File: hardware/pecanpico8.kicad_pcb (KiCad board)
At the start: 4 copper layers, 29.8 x 44.7 mm, 149 parts, among them IC1 SPV1040, IC2 TPS62260, IC3 ADP322ACPZ-115-R7, IC4 Si4464, IC5 STM32F745IGKx, IC6 EVA-7M, IC7 PAC1720, IC8 BME280, IC9 BME280, P1 CONN_02X13, P2 CONN_01X11, P3 USB_OTG, P4 IPX 2mm, P5 CONN_01X02, P6 IPX 2mm, P7 CONN_02X13, Q1 FDN306P, U1 AS-213, U2 LFCN-120, U3 uctronics OV2640, X1 KT2016K26000BCW18ZAS

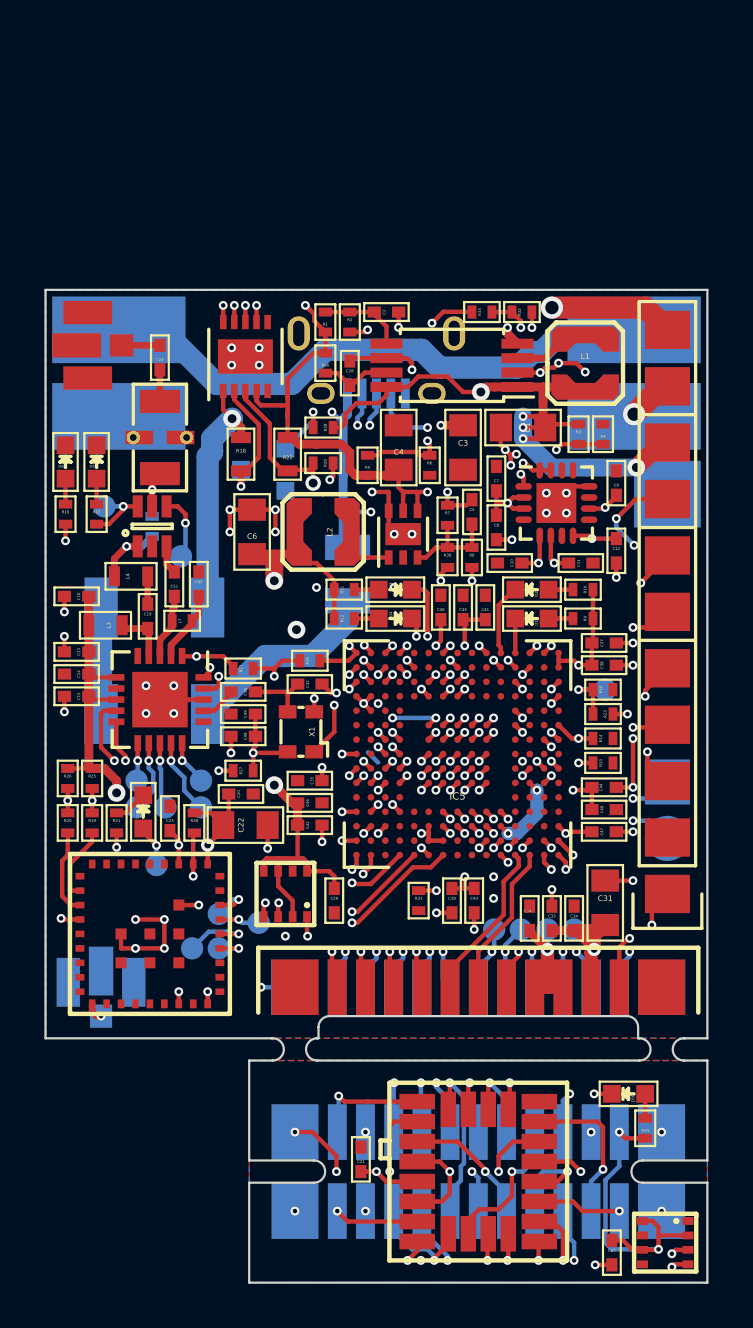
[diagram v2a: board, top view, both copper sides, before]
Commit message: Added new LDO for GPS Implemented constant voltage for LEDs Replaced MicroUSB THT connector with SMD connector Replaced LPF
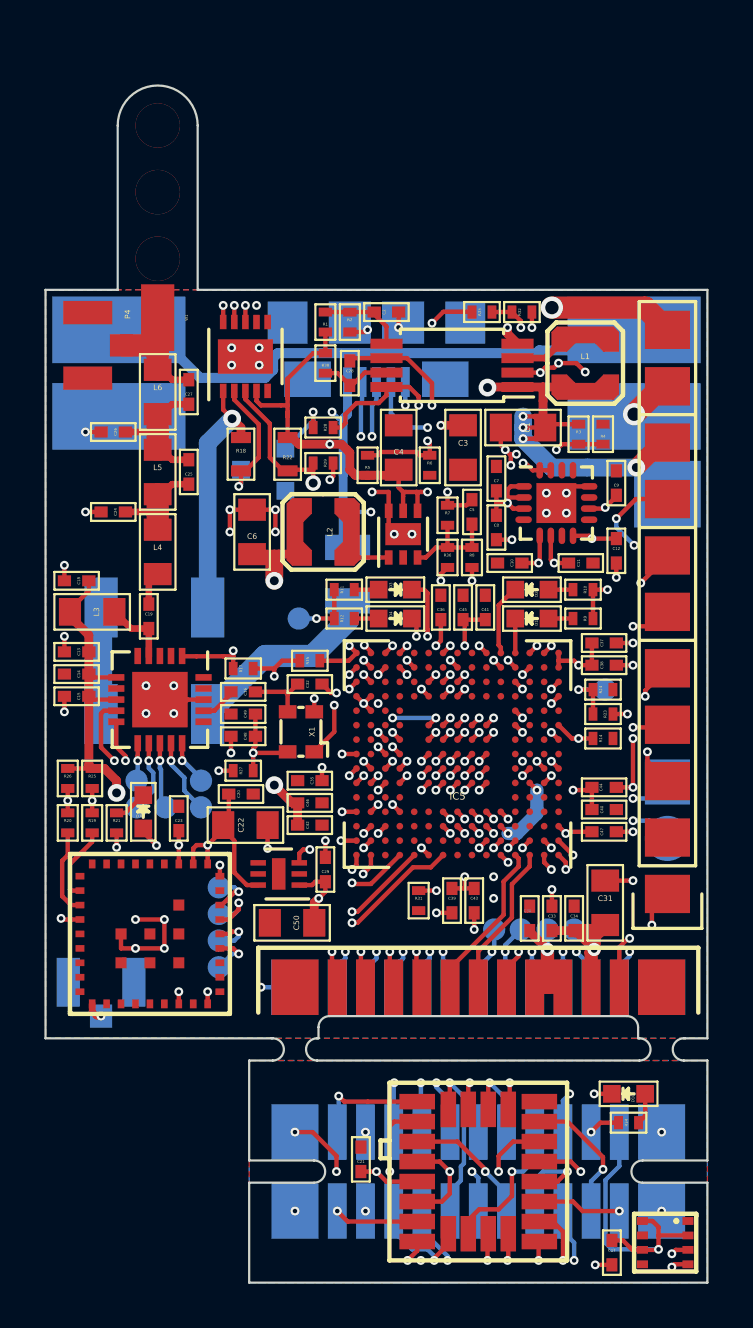
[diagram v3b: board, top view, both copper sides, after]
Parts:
- removed C51: 470p, stm32f7:C_0402
- removed D5: red, stm32f7:LED_0603
- removed D6: green, stm32f7:LED_0603
- removed L7: 56n, stm32f7:R_0402
- removed R13: 100k, stm32f7:R_0402
- removed R15: 1k5, stm32f7:R_0402
- removed R16: 330R, stm32f7:R_0402
- removed R37, R38: 0R, stm32f7:R_0402
- removed U1: AS-213, stm32f7:SC-70-6
- removed U2: LFCN-120, stm32f7:FV1206
- removed W3: Testpad, stm32f7:Testpad
- added C25: 470p, stm32f7:C_0402, F.Cu at (53.5, 99.1)
- added C26: 22p, stm32f7:C_0402, F.Cu at (50.1, 97.3)
- added C27: 470p, stm32f7:C_0402, F.Cu at (53.5, 95.5)
- added L5: 82n, stm32f7:C_0805, F.Cu at (52.1, 99.1)
- added L6: 56n, stm32f7:C_0805, F.Cu at (52.1, 95.5)
- added REF**: MountingHole_2-5mm, Mounting_Holes:MountingHole_2-5mm, F.Cu at (52.1, 89.5)
- added REF**: MountingHole_2-5mm, Mounting_Holes:MountingHole_2-5mm, F.Cu at (52.1, 86.5)
- added REF**: MountingHole_2-5mm, Mounting_Holes:MountingHole_2-5mm, F.Cu at (52.1, 83.5)
- C24: value 470p -> 22p
- C50: value 470p -> 22u; footprint stm32f7:C_0402 -> stm32f7:C_0805
- D1: value green -> yellow
- D2: value green -> blue
- D4: value green -> red
- IC8: value BME280 -> LDLN015PU30R; footprint stm32f7:BME280 -> Housings_DFN_QFN:DFN-6-1EP_2x2mm_Pitch0.5mm
- L3, L4: footprint stm32f7:R_0603 -> stm32f7:C_0805
- P3: value USB_OTG -> ZX62-B-5PA(33); footprint stm32f7:USB_Micro-B -> stm32f7:USB_Micro-B_SMD
- R21: value 1k5 -> 1k
- W1: footprint stm32f7:Testpad -> stm32f7:PAD_3x1.5; moved to F.Cu
- moved C50 15.8 mm to (58.2, 119.4), turned to 180 degrees
- moved W21 12.8 mm to (58.5, 105.7)
- moved W1 8.83 mm to (52.1, 92.2), turned to 90 degrees
- moved C24 7.26 mm to (50.1, 100.9), turned to 180 degrees
- moved W17 1.84 mm to (54.9, 119.0)
- moved L4 1.63 mm to (52.1, 102.7), turned to 270 degrees
- moved C29 1.46 mm to (59.7, 117.0), turned to 90 degrees
- moved W19 1.25 mm to (54.9, 120.2)
- moved W15 1.20 mm to (54.9, 117.8)
- moved IC8 0.95 mm to (57.6, 117.2), turned to 180 degrees
- moved W20 0.85 mm to (54.9, 121.4)
- moved L3 0.85 mm to (49.2, 105.4)
- moved R34 0.79 mm to (73.3, 128.4), turned to 0 degrees
- moved C18 0.70 mm to (48.5, 104.0)
- moved P3 0.50 mm to (62.0, 93.5)
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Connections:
- C20 pad 1: +3V3 -> /VCC_GPS
- C22 pad 1: +3V3 -> /VCC_GPS
- C24 pad 2: Net-(C24-Pad2) -> GND
- C29 pad 1: +1V8 -> VDD
- C3 pad 1: /SENSE_BAT- -> VDD
- C4 pad 1: /SENSE_BAT- -> VDD
- C50 pad 1: GND -> VDD
- C50 pad 2: Net-(C50-Pad2) -> GND
- C7 pad 1: /SENSE_BAT- -> VDD
- C8 pad 1: /SENSE_BAT- -> VDD
- C9 pad 1: /SENSE_BAT- -> VDD
- D7 pad 2: +3V3 -> /VCC_GPS
- IC1 pad 4: /SENSE_BAT- -> VDD
- IC2 pad 4: /SENSE_BAT- -> VDD
- IC2 pad 5: /SENSE_BAT- -> VDD
- IC3 pad 1: /GPS_EN -> VDD
- IC3 pad 10: /SENSE_BAT- -> VDD
- IC3 pad 2: /SENSE_BAT- -> VDD
- IC3 pad 3: /SENSE_BAT- -> VDD
- IC4 pad 19: /RADIO_GPIO2 -> (no net)
- IC4 pad 2: Net-(C50-Pad2) -> (no net)
- IC4 pad 20: /RADIO_GPIO3 -> (no net)
- IC4 pad 3: Net-(C51-Pad1) -> (no net)
- IC5 pad B10: +IO -> (no net)
- IC5 pad B14: (no net) -> /GPS_EN
- IC5 pad B9: +IO -> (no net)
- IC5 pad C10: +IO -> (no net)
- IC5 pad J2: /GPS_EN -> (no net)
- IC5 pad N13: /PAC_ALERT -> (no net)
- IC6 pad 19: +3V3 -> /VCC_GPS
- IC6 pad 20: +IO -> /VCC_GPS
- IC7 pad 10: /SENSE_BAT- -> +3V3
- IC7 pad 4: /SENSE_BAT- -> VDD
- IC7 pad 7: /PAC_ALERT -> (no net)
- IC8 pad 1: GND -> VDD
- IC8 pad 2: +1V8 -> (no net)
- IC8 pad 3: /I2C_SDA -> /GPS_EN
- IC8 pad 4: /I2C_SCL -> GND
- IC8 pad 5: +1V8 -> (no net)
- IC8 pad 6: +1V8 -> /VCC_GPS
- L4 pad 1: Net-(L4-Pad1) -> Net-(C24-Pad1)
- P4 pad 1: Net-(C24-Pad2) -> Net-(C27-Pad2)
- R1 pad 1: /SENSE_BAT- -> VDD
- R10 pad 1: +1V8 -> +3V3
- R11 pad 1: +1V8 -> +3V3
- R12 pad 1: +1V8 -> +3V3
- R22 pad 2: /SENSE_BAT- -> VDD
- R30 pad 2: /SENSE_BAT- -> VDD
- R34 pad 1: +1V8 -> /OV2640_AVDD
- R5 pad 1: /SENSE_BAT- -> VDD
- R9 pad 1: +1V8 -> +3V3
- W1 pad 1: /RADIO_GPIO2 -> Net-(C27-Pad2)
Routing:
- net VDD: track 0.00 -> 69.0 mm, vias 0 -> 7
- net /SENSE_BAT-: track 49.4 -> 0.00 mm, vias 7 -> 0
- net /PAC_ALERT: track 22.8 -> 0.00 mm, vias 4 -> 0
- net /RADIO_GPIO3: track 20.9 -> 0.00 mm, vias 3 -> 0
- net /RADIO_GPIO2: track 18.6 -> 0.00 mm, vias 2 -> 0
- net +IO: track 16.2 -> 0.00 mm, vias 2 -> 0
- net +1V8: track 164.4 -> 148.9 mm, vias 33 -> 32
- net /GPS_EN: track 17.8 -> 4.84 mm, vias 3 -> 2
- net /VCC_GPS: track 0.00 -> 12.1 mm, vias 0 -> 2
- net Net-(C25-Pad2): track 0.00 -> 6.22 mm
- net Net-(C27-Pad2): track 0.00 -> 5.69 mm
- net +3V3: track 36.2 -> 40.9 mm, vias 4 -> 5
- net /I2C_SCL: track 63.4 -> 59.4 mm, vias 5 -> 4
- net Net-(L4-Pad1): track 3.41 -> 0.00 mm, vias 1 -> 0
- net +SOL: track 53.7 -> 50.4 mm, vias 6 -> 7
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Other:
- board size 29.8 x 44.7 mm -> 29.8 x 53.9 mm
- net class Power: clearance 0.1 -> 0.15; trace_width 0.2 -> 0.45
- board text added: "+3.3V"
- board text added: "March 2017"
- board text removed: "Jan 2017"
- board text removed: "VCC GPS"

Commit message: Moving parts around
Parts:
- moved D9 6.81 mm to (51.7, 103.2)
- moved F1 5.50 mm to (56.3, 100.4)
- moved D8 5.21 mm to (51.7, 100.0)
- moved C50 3.40 mm to (61.5, 118.4), turned to 0 degrees
- moved C29 2.90 mm to (57.6, 119.0), turned to 180 degrees
- moved Q1 2.78 mm to (55.5, 96.6)
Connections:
- D8 pad 1: +SOL -> Net-(D8-Pad1)
- D9 pad 2: Net-(D9-Pad2) -> /USB_VUSB
- F1 pad 1: Net-(D9-Pad2) -> Net-(D8-Pad1)
- F1 pad 2: /USB_VUSB -> +SOL
- IC5 pad A11: /GPS_RESET -> /GPS_TIMEPULSE
- IC5 pad A9: /GPS_TIMEPULSE -> /GPS_RESET
- IC9 pad 5: GND -> +1V8
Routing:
- net Net-(D9-Pad2): track 8.94 -> 0.00 mm
- net /USB_VUSB: track 25.7 -> 33.3 mm
- net /SWD_SWCLK: track 24.0 -> 18.0 mm
- net +SOL: track 50.4 -> 44.6 mm
- net Net-(D8-Pad1): track 0.00 -> 2.98 mm
- net /SENSE_SOL-: track 6.04 -> 8.13 mm
- net /GPS_RESET: track 11.4 -> 13.4 mm
- net Net-(D8-Pad2): track 4.80 -> 3.20 mm
- net GND: track 88.0 -> 86.4 mm, vias 110 -> 107
- net /CAM_D9: track 8.84 -> 10.2 mm
- net /GPS_TIMEPULSE: track 23.8 -> 22.5 mm
- net /SWD_SWDIO: track 18.9 -> 17.6 mm
- net /SOL_SHORT_EN: track 18.6 -> 19.7 mm
- net /CAM_EN: track 17.9 -> 16.9 mm
- net VDD: track 69.0 -> 69.8 mm
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
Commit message: Moving parts around
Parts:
- moved C25 4.20 mm to (49.4, 99.1)
- moved C24 1.41 mm to (48.8, 100.7)
- moved C26 1.41 mm to (48.8, 97.5)
- moved L5 1.40 mm to (50.8, 99.1)
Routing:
- net GND: track 86.4 -> 88.6 mm, vias 107 -> 110
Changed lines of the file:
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@@
     (links 460)
     (no_connects 2)
-    (area 37.303263 78.92488 87.9 135.843)
+    (area 47.049999 81.649999 76.950001 135.650001)
     (thickness 1)
     (drawings 85)
-    (tracks 1869)
+    (tracks 1881)
     (zones 0)
     (modules 145)
@@
     (add_net "Net-(W6-Pad1)")
   )
+  (module stm32f7:PAD_6x3 (layer B.Cu)
+    (at 50.4 96.6)
+    (fp_text reference W10 (at 0 -3) (layer B.SilkS) hide
+      (effects (font (size 0.5 0.5) (thickness 0.075)) (justify mirror))
+    )
+    (fp_text value Pad (at 0 -2.2) (layer B.Fab) hide
+      (effects (font (size 0.5 0.5) (thickness 0.075)) (justify mirror))
+    )
+    (pad 1 smd rect (at 0 0) (size 6 3) (layers B.Cu B.Mask)
+      (net 2 GND) (zone_connect 2))
+  )
   (module stm32f7:Pin_Header_Straight_1x11 (layer F.Cu)
     (at 75.1 118.1 180)
@@
       (net 83 /BATT_CONN))
   )
-  (module stm32f7:PAD_6x3 (layer B.Cu)
-    (at 50.4 96.6)
-    (fp_text reference W10 (at 0 -3) (layer B.SilkS) hide
-      (effects (font (size 0.5 0.5) (thickness 0.075)) (justify mirror))
-    )
-    (fp_text value Pad (at 0 -2.2) (layer B.Fab) hide
-      (effects (font (size 0.5 0.5) (thickness 0.075)) (justify mirror))
-    )
-    (pad 1 smd rect (at 0 0) (size 6 3) (layers B.Cu B.Mask)
-      (net 2 GND) (zone_connect 2))
-  )
   (module stm32f7:R_0402 (layer F.Cu)
     (at 61.6 98.8 90)
@@
   )
   (module stm32f7:C_0402 (layer F.Cu)
-    (at 53.55 99.1 90)
+    (at 49.35 99.1 90)
     (descr "Capacitor SMD 0402, reflow soldering, AVX (see smccp.pdf)")
     (tags "capacitor 0402")
@@
   )
   (module stm32f7:C_0402 (layer F.Cu)
-    (at 50.15 97.3 180)
+    (at 48.75 97.5 180)
     (descr "Capacitor SMD 0402, reflow soldering, AVX (see smccp.pdf)")
     (tags "capacitor 0402")
@@
   )
   (module stm32f7:C_0805 (layer F.Cu)
-    (at 52.15 99.1 270)
+    (at 50.75 99.1 270)
     (descr "Capacitor SMD 0805, reflow soldering, AVX (see smccp.pdf)")
     (tags "capacitor 0805")
@@
   )
   (module stm32f7:C_0402 (layer F.Cu)
-    (at 50.15 100.9 180)
+    (at 48.75 100.7 180)
     (descr "Capacitor SMD 0402, reflow soldering, AVX (see smccp.pdf)")
     (tags "capacitor 0402")
@@
   (module stm32f7:PAD_3x1.5 (layer F.Cu)
     (at 52.15 92.15 90)
-    (fp_text reference W1 (at 0 1.3 90) (layer F.SilkS)
+    (fp_text reference W1 (at 0 1.3 90) (layer F.SilkS) hide
       (effects (font (size 0.127 0.127) (thickness 0.01875)))
     )
@@
   (module stm32f7:IPX_2mm (layer F.Cu)
     (at 49 93.4)
-    (fp_text reference P4 (at 1.8 -1.4 270) (layer F.SilkS)
+    (fp_text reference P4 (at 1.8 -1.4 90) (layer F.SilkS) hide
       (effects (font (size 0.25 0.25) (thickness 0.0375)))
     )
@@
   (segment (start 65.4 117.85) (end 65.975 117.85) (width 0.2) (layer F.Cu) (net 1))
   (segment (start 65.975 117.325) (end 65.975 117.85) (width 0.2) (layer F.Cu) (net 1))
+  (segment (start 48.2 97.5) (end 48.2 96.9) (width 0.2) (layer F.Cu) (net 2))
+  (segment (start 48.2 96.9) (end 48.1 96.8) (width 0.2) (layer F.Cu) (net 2))
+  (via (at 48.1 96.8) (size 0.4) (drill 0.2) (layers F.Cu B.Cu) (net 2))
+  (segment (start 48.2 100.7) (end 48.2 100.1) (width 0.2) (layer F.Cu) (net 2))
+  (segment (start 48.2 100.1) (end 48.1 100) (width 0.2) (layer F.Cu) (net 2))
+  (via (at 48.1 100) (size 0.4) (drill 0.2) (layers F.Cu B.Cu) (net 2))
+  (segment (start 48.2 97.5) (end 48.2 98.1) (width 0.2) (layer F.Cu) (net 2))
+  (segment (start 48.2 98.1) (end 48.1 98.2) (width 0.2) (layer F.Cu) (net 2))
+  (via (at 48.1 98.2) (size 0.4) (drill 0.2) (layers F.Cu B.Cu) (net 2))
+  (segment (start 48.2 100.7) (end 48.2 101.3) (width 0.2) (layer F.Cu) (net 2))
+  (segment (start 48.2 101.3) (end 48.1 101.4) (width 0.2) (layer F.Cu) (net 2))
+  (via (at 48.1 101.4) (size 0.4) (drill 0.2) (layers F.Cu B.Cu) (net 2))
   (segment (start 49.85 123.05) (end 49.85 122.5) (width 0.2) (layer F.Cu) (net 2))
   (via (at 49.85 122.5) (size 0.4) (drill 0.2) (layers F.Cu B.Cu) (net 2))
@@
   (segment (start 63.3 95.05) (end 63.3 96.1) (width 0.2) (layer B.Cu) (net 2))
   (via (at 63.3 96.1) (size 0.4) (drill 0.2) (layers F.Cu B.Cu) (net 2))
-  (segment (start 48.9 97.3) (end 49.6 97.3) (width 0.2) (layer F.Cu) (net 2))
-  (via (at 48.9 97.3) (size 0.4) (drill 0.2) (layers F.Cu B.Cu) (net 2))
   (segment (start 54.95 117.3) (end 54.95 116.8) (width 0.2) (layer F.Cu) (net 2))
   (via (at 54.95 116.8) (size 0.4) (drill 0.2) (layers F.Cu B.Cu) (net 2))
@@
   (segment (start 75.1 95.24) (end 75.04 95.24) (width 1) (layer F.Cu) (net 83))
   (segment (start 74.9476 95.24) (end 75.1 95.24) (width 1) (layer F.Cu) (net 83))
-  (segment (start 52.15 100.1) (end 52.15 100.9) (width 1) (layer F.Cu) (net 84))
-  (segment (start 52.15 100.9) (end 52.15 101.7) (width 1) (layer F.Cu) (net 84))
-  (segment (start 50.7 100.9) (end 52.15 100.9) (width 0.3) (layer F.Cu) (net 84))
-  (segment (start 53.55 99.65) (end 52.8 99.65) (width 0.3) (layer F.Cu) (net 84))
-  (segment (start 52.15 100.1) (end 52.35 100.1) (width 0.3) (layer F.Cu) (net 84))
-  (segment (start 52.35 100.1) (end 52.8 99.65) (width 0.3) (layer F.Cu) (net 84))
+  (segment (start 49.35 99.65) (end 49.35 100.1) (width 0.4) (layer F.Cu) (net 84))
+  (segment (start 49.35 100.1) (end 49.35 100.65) (width 0.4) (layer F.Cu) (net 84))
+  (segment (start 50.75 100.1) (end 49.35 100.1) (width 0.4) (layer F.Cu) (net 84))
+  (segment (start 49.35 100.65) (end 49.3 100.7) (width 0.4) (layer F.Cu) (net 84))
+  (segment (start 50.75 100.3) (end 51.2 100.75) (width 1) (layer F.Cu) (net 84))
+  (segment (start 51.2 100.75) (end 52.15 101.7) (width 1) (layer F.Cu) (net 84))
+  (segment (start 50.75 100.1) (end 50.75 100.3) (width 1) (layer F.Cu) (net 84))
   (segment (start 68.4 116.866002) (end 68.4 116.5) (width 0.2) (layer F.Cu) (net 85))
   (segment (start 68.25 116.35) (end 68.4 116.5) (width 0.2) (layer F.Cu) (net 85))
@@
   (segment (start 68.15 100.75) (end 67.9 100.5) (width 0.2) (layer F.Cu) (net 110))
   (via (at 67.9 100.5) (size 0.4) (drill 0.2) (layers F.Cu B.Cu) (net 110))
-  (segment (start 52.15 96.5) (end 52.15 97.3) (width 1) (layer F.Cu) (net 111))
-  (segment (start 52.15 97.3) (end 52.15 98.1) (width 1) (layer F.Cu) (net 111))
-  (segment (start 50.7 97.3) (end 52.15 97.3) (width 0.3) (layer F.Cu) (net 111))
-  (segment (start 53.55 98.55) (end 52.8 98.55) (width 0.3) (layer F.Cu) (net 111))
-  (segment (start 52.15 98.1) (end 52.35 98.1) (width 0.3) (layer F.Cu) (net 111))
-  (segment (start 52.35 98.1) (end 52.8 98.55) (width 0.3) (layer F.Cu) (net 111))
+  (segment (start 49.35 98.55) (end 49.35 98.1) (width 0.4) (layer F.Cu) (net 111))
+  (segment (start 49.35 98.1) (end 49.35 97.55) (width 0.4) (layer F.Cu) (net 111))
+  (segment (start 50.75 98.1) (end 49.35 98.1) (width 0.4) (layer F.Cu) (net 111))
+  (segment (start 49.35 97.55) (end 49.3 97.5) (width 0.4) (layer F.Cu) (net 111))
+  (segment (start 50.75 97.9) (end 51.2 97.45) (width 1) (layer F.Cu) (net 111))
+  (segment (start 51.2 97.45) (end 52.15 96.5) (width 1) (layer F.Cu) (net 111))
+  (segment (start 50.75 98.1) (end 50.75 97.9) (width 1) (layer F.Cu) (net 111))
   (segment (start 53.55 96.05) (end 52.8 96.05) (width 0.3) (layer F.Cu) (net 111))
   (segment (start 52.15 96.5) (end 52.35 96.5) (width 0.3) (layer F.Cu) (net 111))

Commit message: Moved signals around, created GERBERs
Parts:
- moved IC9 54.8 mm to (58.2, 81.7), turned to 180 degrees
- moved C17 54.3 mm to (60.6, 81.2), turned to 90 degrees
- moved C21 45.8 mm to (71.9, 85.5), turned to 270 degrees
- moved P7 45.7 mm to (66.6, 84.9), turned to 0 degrees
- moved U3 45.7 mm to (66.6, 84.9), turned to 90 degrees
- moved R34 43.5 mm to (59.8, 87.1), turned to 180 degrees
- moved D10 41.0 mm to (59.8, 88.4), turned to 180 degrees
- moved REF** 1.80 mm to (52.1, 87.7)
- moved REF** 1.80 mm to (52.1, 84.7)
- moved REF** 1.80 mm to (52.1, 81.7)
- moved R33 0.91 mm to (65.8, 91.9)
- moved R32 0.80 mm to (67.8, 91.9)
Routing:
- net GND: track 88.6 -> 91.7 mm, vias 110 -> 115
- net +BATT: track 30.8 -> 33.7 mm
- net VDD: track 69.8 -> 69.0 mm
- net /SWD_SWDIO: track 17.6 -> 18.2 mm
- net /USB_VUSB: track 33.3 -> 32.8 mm
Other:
- board size 29.8 x 53.9 mm -> 29.8 x 44.7 mm
